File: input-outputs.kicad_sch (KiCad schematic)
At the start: 4 parts, among them J3 swd, J5 I2C-STEMMA-QT, J9 UART

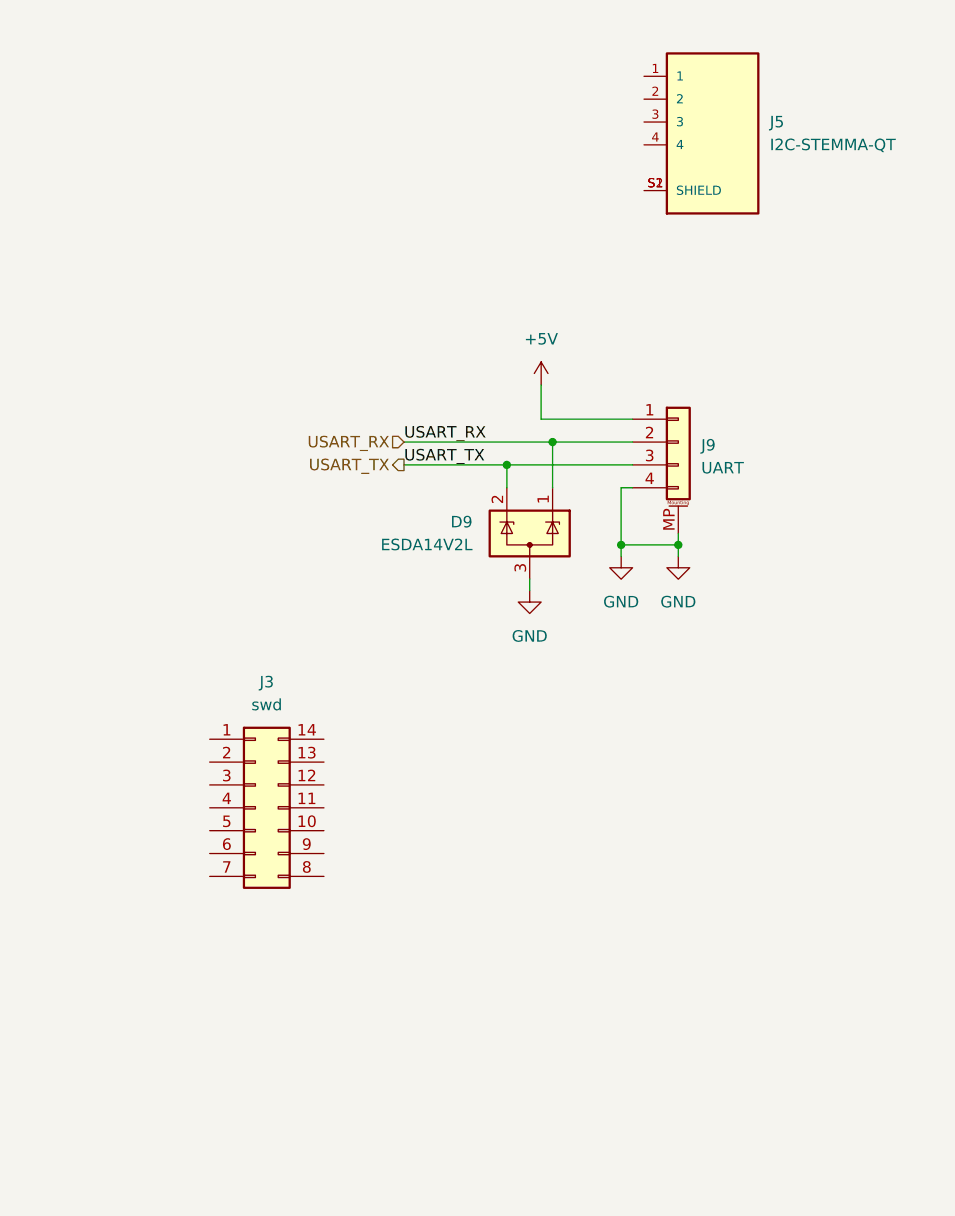
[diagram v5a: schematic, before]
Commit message: All clear (need to verify). LCD backlight driver left untracked
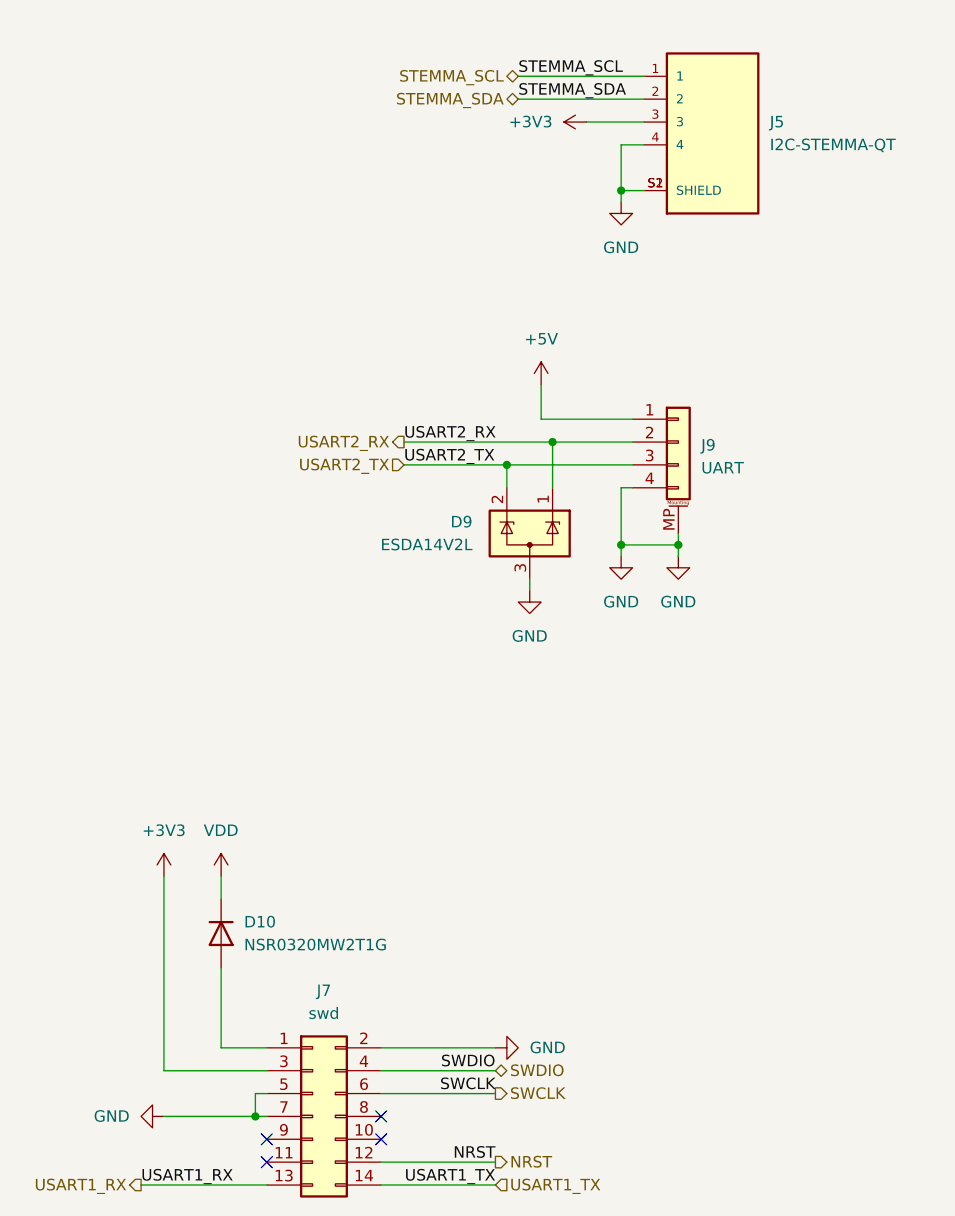
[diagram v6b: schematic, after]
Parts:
- removed J3: swd, Connector_PinHeader_1.27mm:PinHeader_2x07_P1.27mm_Vertical_SMD, symbol Connector_Generic:Conn_02x07_Counter_Clockwise
- added D10: NSR0320MW2T1G, Diode_SMD:D_SOD-323, symbol Device:D
- added J7: swd, Connector_PinHeader_1.27mm:PinHeader_2x07_P1.27mm_Vertical_SMD, symbol Connector_Generic:Conn_02x07_Odd_Even
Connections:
- net GND: now also J5.4, J5.S1 (SHIELD), J5.S2 (SHIELD), J7.2 (Pin_2), J7.5 (Pin_5), J7.7 (Pin_7)
- net STEMMA_SCL: now reaches J5.1
- net STEMMA_SDA: now reaches J5.2
- net +3V3: now reaches J5.3
- net +3V3: now also J7.3 (Pin_3)
- net USART_RX renamed USART2_RX
- net USART_TX renamed USART2_TX
- new net: D10.2 (A), J7.1 (Pin_1)
- new net NRST: J7.12 (Pin_12)
- new net SWCLK: J7.6 (Pin_6)
- new net SWDIO: J7.4 (Pin_4)
- new net USART1_RX: J7.13 (Pin_13)
- new net USART1_TX: J7.14 (Pin_14)
- new net VDD: D10.1 (K)
- no-connect marks 0 -> 4

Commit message: Finished. 1st version, ordered 1st batch
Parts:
- added C50: 1u, Capacitor_SMD:C_0603_1608Metric, symbol Device:C
- D10: JLCPCB Part # (none) -> C48192
- D9: JLCPCB Part # (none) -> C2682282
- J7: JLCPCB Part # (none) -> C2881912
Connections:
- net +3V3: now also C50.1
- net GND: now also C50.2
